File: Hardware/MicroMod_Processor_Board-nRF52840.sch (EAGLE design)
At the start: 33 parts, among them J1 MICROMOD-2222, U1 ARTEMIS_MODULESMD, U2 TSV524, U6 CH340E_MSOP10, Y1 32.768kHz

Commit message: Renamed eagle files appropriately
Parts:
- removed C11, C13: 15pF, SparkFun-Capacitors:15PF-0402T-50V-5%
- removed C20, C21: 0.1uF, SparkFun-Capacitors:0.1UF-0402T-16V-10%
- removed C28: 1.0nF, SparkFun-Capacitors:1.0NF/1000PF-0402_TIGHT-50V-10%
- removed R14, R6: 100k, SparkFun-Resistors:100KOHM-0402T-1/16W-1%
- removed R15: 220KOHM-0402T-1/16W-1%, SparkFun-Resistors:220KOHM-0402T-1/16W-1%
- removed R4, R5, R7: 150k, SparkFun-Resistors:150KOHM-0402T-1/16W-1%
- added C2, C3: 15pF, SparkFun-Capacitors:15PF-0402-50V-5%
- added C4, C5: 10uF, SparkFun-Capacitors:10UF-0402T-6.3V-20%
- added C6: 0.1uF, SparkFun-Capacitors:0.1UF-0402-16V-10%
- C1: device SparkFun-Capacitors:0.1UF-0402T-16V-10% -> SparkFun-Capacitors:0.1UF-0402-16V-10%
- R2, R3: value 100k -> 27; device SparkFun-Resistors:100KOHM-0402T-1/16W-1% -> SparkFun-Resistors:27OHM-0603-1/10W-1%
- U1: value ARTEMIS_MODULESMD -> W25QXX128MBIT-6X5; device SparkFun-IC-Microcontroller:ARTEMIS_MODULESMD -> SparkFun-MicroMod:W25QXX128MBIT-6X5
- U2: value TSV524 -> MDBT50Q; device OpAmp:TSV524 -> nrf52840:MDBT50Q
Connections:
- removed net ADC0_BUFF1: R3.2, U2G1.-IN, U2G1.OUT
- removed net ADC0_BUFF2: R3.1, R5.2, U2G2.+IN
- removed net ADC1_BUFF2: R6.1, R7.2, U2G3.+IN
- removed net ADC_BUFF1: R6.2, U2G4.-IN, U2G4.OUT
- removed net N$7: C11.2, U1.XO, Y1.2
- removed net SCALED_ADC0: U1.~AD32(SCCIO), U2G2.-IN, U2G2.OUT
- removed net SCALED_ADC1: U1.~AD35(TX1/I2SDAT/PDMCLK), U2G3.-IN, U2G3.OUT
- removed net SCALED_BATT_VIN/3: R2.1, R4.2, U1.~AD31(SCCCLK)
- new net N$1: R2.2, U2.D+
- new net N$3: R3.2, U2.D-
- net !RESET!: no longer C20.2, C28.1, R14.1, U1.!RST
- net !RTS: no longer C20.1, C21.1
- net 3.3V: now also C4.1, C5.1, C6.1, U1.VDD, U2.VDD, U2.VDDH; no longer R14.2, U1.VDD*2, U2G5.V+
- net 3.3V_EN: no longer U1.(SLNCE/I2SWCLK)D3
- net ADC0: no longer U2G1.+IN
- net ADC1: no longer U2G4.+IN
- net ADC_D+: no longer U1.~AD13(I2SBCLK/RX1)
- net ADC_D-: no longer U1.~AD12(PDMCLK/TX1)
- net BATT_VIN/3: no longer R2.2
- net BOOT: no longer C21.2, R15.2, U1.~BOOT(MOSI5/RX1/32KHZ)
- net CAM_PCLK: no longer U1.~AD11(PDMDATA)
- net CLKOUT: no longer U1.(SLSCK/SLSCL/CLKOUT)D0
- net CTS1: no longer U1.(CMPRF1/TRIG1/SCCCLK)D17
- net D0: no longer U1.(SLMOSI/SLSDA)D1
- net D1: no longer U1.(SLMISO)D2
- net GND: now also C2.1, C3.1, C4.2, C5.2, C6.2, U1.GND, U2.GND; no longer C11.1, C13.1, C28.2, R15.1, R4.1, R5.1, R7.1, U1.GND*6, U2G5.V-
- net GPIO0: no longer U1.AD16(TRIG0/SCCRST)
- net GPIO1: no longer U1.~AD33(SWO/32KHZ)
- net GPIO2: no longer U1.AD34(CMPRF2/PDMDATA)
- net GPIO3: no longer U1.(SCL2/SCK2)~D27
- net GPIO4: no longer U1.(MOSI2/I2SWCLK)~D28
- net GPIO5: no longer U1.~AD29(PDMDATA)
- net GPIO6: no longer U1.(ADCD1P/TX1/PDMCLK)D14
- net GPIO7: no longer U1.(ADCD1N/RX1/PDMDATA)D15
- net I2C_!INT!: no longer U1.(CMPIN1/SCCIO)~D18
- net LED_BUILTIN: no longer U1.(CMPRF0/SCCCLK/I2SBCLK)~D19
- net N$4: now also C3.2, U2.P0.00(XL1), Y1.1; no longer U1.XI
- net N$5: now also C2.2, U2.P0.01(XL2), Y1.2; no longer C13.2, Y1.1
- net PDM_CLK: no longer U1.(TX1/PDMCLK/SCCIO)~D37
- net PDM_DATA: no longer U1.(RX1/TRIG1/PDMDATA)D36
- net PWM0: no longer U1.(MOSI4)~D44
- net PWM1: no longer U1.(SWO/I2SDAT/PDMDATA)~D45
- net RTS1: no longer U1.(MOSI1/TX1/PDMCLK)D10
- net RX1: no longer U1.(SDA2/MISO2/RX1)~D25
- net RXI-0: no longer U1.~D49(RX0/SDA5/MISO5)
- net SCL: no longer U1.(SCL4/SCK4/TX1)~D39
- net SCL1: no longer U1.(SCL1/SCK1/TX1/SCCLK)D8
- net SDA: no longer U1.(SDA4/MISO4/RX1)D40
- net SDA1: no longer U1.(SDA1/MISO1/RX1/SCCIO)D9
- net SDIO_DATA1: no longer U1.(SCCRST)~D26
- net SDIO_DATA2: no longer U1.(RX1/SLINT)~D4
- net SPI_!CS!: no longer U1.(I2SWCLK/CMPOUT)~D23
- net SPI_!CS!1: no longer U1.(BLEIF_IRQ/SWO/I2SWCLK)D41
- net SPI_MISO: no longer U1.(PDMCLK/SWO)~D22, U1.(SDA0/MISO0/I2SDAT)~D6
- net SPI_MISO1: no longer U1.(SDA3/MISO3/RX1)~D43
- net SPI_MOSI: no longer U1.(MOSI0/CLKOUT)~D7
- net SPI_MOSI1: no longer U1.(MOSI3/RX1)D38
- net SPI_SCK: no longer U1.(SCL0/SCK0)~D5
- net SPI_SCK1: no longer U1.(SCL3/SCK3/TX1)~D42
- net SWDCK: now also U2.SWDCLK; no longer U1.D20(SWDCK/TX1)
- net SWDIO: now also U2.SWDIO; no longer U1.D21(SWDIO/RX1/SCCRST)
- net TX1: no longer U1.(TX1/32KHZ/SWO)~D24
- net TXO-0: no longer U1.~D48(TX0/SCL5/SCK5)
- net USB_D+: now also R2.1
- net USB_D-: now also R3.1
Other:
- note added: "128Mb Flash"
- note added: "MicroMod-nRF52840-Processor-Board"
- note added: "Paul Clark"
- note added: "Priyanka Makin"
- note added: "v1.0"
- note removed: "3.3V to 2V Scaling"
- note removed: "Artemis"
- note removed: "Bootloader Reset Circuit"
- note removed: "N. Seidle"
- note removed: "v1.2"
- moved on the sheet: C1, C17, C18, D2, D7, J1, R1, R2, R3, U6, Y1

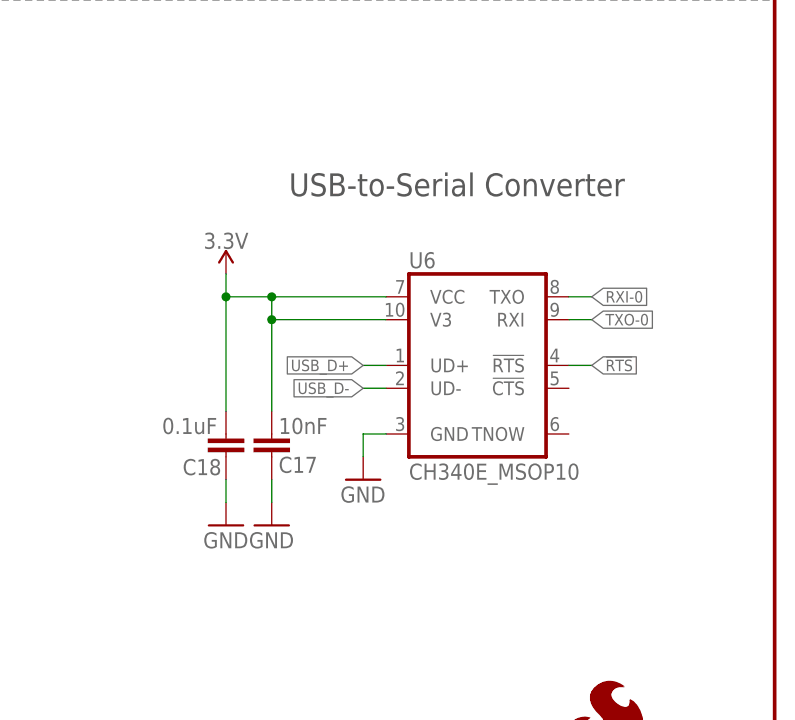
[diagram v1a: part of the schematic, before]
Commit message: Ripped up old traces
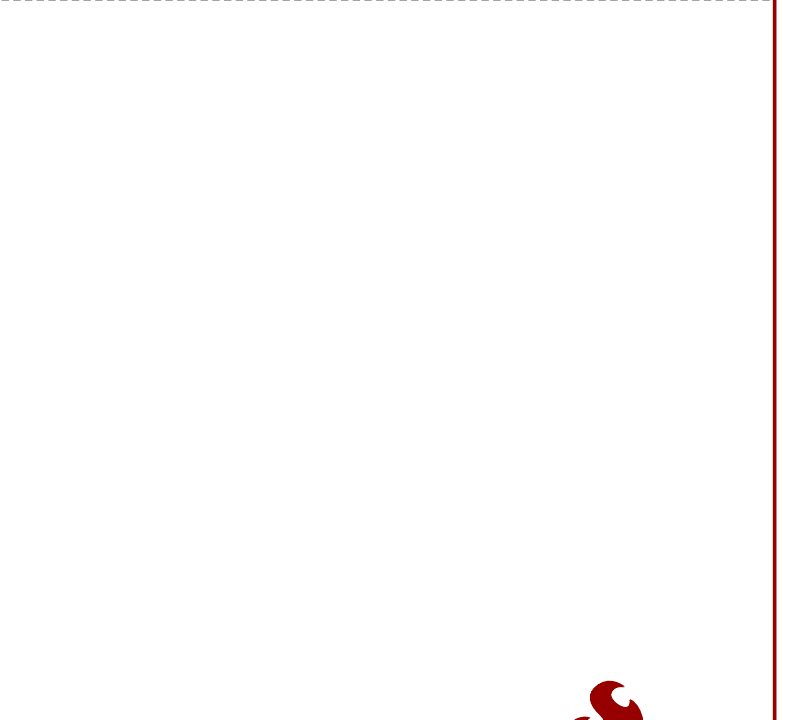
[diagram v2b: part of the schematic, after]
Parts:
- removed C17: 10nF, SparkFun-Capacitors:10NF-0402T-25V-10%
- removed C18: 0.1uF, SparkFun-Capacitors:0.1UF-0402T-16V-10%
- removed U6: CH340E_MSOP10, SparkFun-IC-Comms:CH340E_MSOP10
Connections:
- removed net !RTS: U6.!RTS
- removed net RXI-0: U6.TXO
- removed net TXO-0: U6.RXI
- net 3.3V: no longer C17.1, C18.1, U6.V3, U6.VCC
- net GND: no longer C17.2, C18.2, U6.GND
- net USB_D+: no longer U6.UD+
- net USB_D-: no longer U6.UD-
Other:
- note removed: "USB-to-Serial Converter"
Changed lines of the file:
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@@
 <part name="R1" library="SparkFun-Resistors" deviceset="1KOHM" device="-0402T-1/16W-1%" value="1k"/>
 <part name="GND3" library="SparkFun-PowerSymbols" deviceset="GND" device=""/>
-<part name="GND31" library="SparkFun-PowerSymbols" deviceset="GND" device=""/>
-<part name="C17" library="SparkFun-Capacitors" deviceset="10NF" device="-0402T-25V-10%" value="10nF"/>
-<part name="GND33" library="SparkFun-PowerSymbols" deviceset="GND" device=""/>
-<part name="C18" library="SparkFun-Capacitors" deviceset="0.1UF" device="-0402T-16V-10%" value="0.1uF"/>
-<part name="GND38" library="SparkFun-PowerSymbols" deviceset="GND" device=""/>
-<part name="SUPPLY26" library="SparkFun-PowerSymbols" deviceset="3.3V" device=""/>
-<part name="U6" library="SparkFun-IC-Comms" deviceset="CH340E" device="_MSOP10"/>
 <part name="FD1" library="SparkFun-Aesthetics" deviceset="FIDUCIAL" device="UFIDUCIAL" value="FIDUCIALUFIDUCIAL"/>
 <part name="FD2" library="SparkFun-Aesthetics" deviceset="FIDUCIAL" device="UFIDUCIAL" value="FIDUCIALUFIDUCIAL"/>
@@
 <sheet>
 <plain>
-<text x="396.494" y="116.586" size="2.54" layer="97" font="vector" align="center">USB-to-Serial Converter</text>
 <text x="53.594" y="271.526" size="2.54" layer="94" font="vector" align="center">MicroMod Connector</text>
 <wire x1="0" y1="137.16" x2="104.14" y2="137.16" width="0.2032" layer="97" style="longdash"/>
@@
 <attribute name="VALUE" x="60.96" y="83.566" size="1.778" layer="96" align="top-center"/>
 </instance>
-<instance part="GND31" gate="1" x="370.84" y="78.74" smashed="yes">
-<attribute name="VALUE" x="368.3" y="76.2" size="1.778" layer="96"/>
-</instance>
-<instance part="C17" gate="G$1" x="375.92" y="86.36" smashed="yes">
-<attribute name="NAME" x="376.682" y="84.582" size="1.778" layer="95"/>
-<attribute name="VALUE" x="376.682" y="88.9" size="1.778" layer="96"/>
-</instance>
-<instance part="GND33" gate="1" x="375.92" y="78.74" smashed="yes">
-<attribute name="VALUE" x="373.38" y="76.2" size="1.778" layer="96"/>
-</instance>
-<instance part="C18" gate="G$1" x="370.84" y="86.36" smashed="yes">
-<attribute name="NAME" x="366.014" y="84.328" size="1.778" layer="95"/>
-<attribute name="VALUE" x="363.728" y="88.9" size="1.778" layer="96"/>
-</instance>
-<instance part="GND38" gate="1" x="386.08" y="83.82" smashed="yes">
-<attribute name="VALUE" x="383.54" y="81.28" size="1.778" layer="96"/>
-</instance>
-<instance part="SUPPLY26" gate="G$1" x="370.84" y="106.68" smashed="yes">
-<attribute name="VALUE" x="370.84" y="109.474" size="1.778" layer="96" align="bottom-center"/>
-</instance>
-<instance part="U6" gate="U1" x="398.78" y="96.52" smashed="yes">
-<attribute name="NAME" x="391.16" y="107.315" size="1.778" layer="95"/>
-<attribute name="VALUE" x="391.16" y="83.82" size="1.778" layer="96"/>
-</instance>
 <instance part="FD1" gate="G$1" x="429.26" y="25.4" smashed="yes"/>
 <instance part="FD2" gate="G$1" x="426.72" y="25.4" smashed="yes"/>
@@
 <net name="3.3V" class="0">
 <segment>
-<pinref part="C18" gate="G$1" pin="1"/>
-<wire x1="370.84" y1="106.68" x2="370.84" y2="104.14" width="0.1524" layer="91"/>
-<wire x1="370.84" y1="104.14" x2="370.84" y2="91.44" width="0.1524" layer="91"/>
-<wire x1="388.62" y1="104.14" x2="375.92" y2="104.14" width="0.1524" layer="91"/>
-<junction x="370.84" y="104.14"/>
-<pinref part="SUPPLY26" gate="G$1" pin="3.3V"/>
-<pinref part="U6" gate="U1" pin="VCC"/>
-<wire x1="375.92" y1="104.14" x2="370.84" y2="104.14" width="0.1524" layer="91"/>
-<wire x1="388.62" y1="101.6" x2="375.92" y2="101.6" width="0.1524" layer="91"/>
-<pinref part="C17" gate="G$1" pin="1"/>
-<wire x1="375.92" y1="91.44" x2="375.92" y2="101.6" width="0.1524" layer="91"/>
-<pinref part="U6" gate="U1" pin="V3"/>
-<wire x1="375.92" y1="101.6" x2="375.92" y2="104.14" width="0.1524" layer="91"/>
-<junction x="375.92" y="101.6"/>
-<junction x="375.92" y="104.14"/>
-</segment>
-<segment>
 <wire x1="12.7" y1="241.3" x2="12.7" y2="254" width="0.1524" layer="91"/>
 <wire x1="30.48" y1="241.3" x2="12.7" y2="241.3" width="0.1524" layer="91"/>
@@
 <pinref part="GND3" gate="1" pin="GND"/>
 <wire x1="60.96" y1="86.36" x2="60.96" y2="88.9" width="0.1524" layer="91"/>
-</segment>
-<segment>
-<wire x1="370.84" y1="83.82" x2="370.84" y2="81.28" width="0.1524" layer="91"/>
-<pinref part="GND31" gate="1" pin="GND"/>
-<pinref part="C18" gate="G$1" pin="2"/>
-</segment>
-<segment>
-<pinref part="C17" gate="G$1" pin="2"/>
-<pinref part="GND33" gate="1" pin="GND"/>
-<wire x1="375.92" y1="81.28" x2="375.92" y2="83.82" width="0.1524" layer="91"/>
-</segment>
-<segment>
-<wire x1="388.62" y1="88.9" x2="386.08" y2="88.9" width="0.1524" layer="91"/>
-<wire x1="386.08" y1="88.9" x2="386.08" y2="86.36" width="0.1524" layer="91"/>
-<pinref part="GND38" gate="1" pin="GND"/>
-<pinref part="U6" gate="U1" pin="GND"/>
 </segment>
 <segment>
@@
 </segment>
 </net>
-<net name="RXI-0" class="0">
-<segment>
-<label x="411.48" y="104.14" size="1.27" layer="95" font="vector" xref="yes"/>
-<wire x1="408.94" y1="104.14" x2="411.48" y2="104.14" width="0.1524" layer="91"/>
-<pinref part="U6" gate="U1" pin="TXO"/>
-</segment>
-</net>
-<net name="TXO-0" class="0">
-<segment>
-<label x="411.48" y="101.6" size="1.27" layer="95" font="vector" xref="yes"/>
-<wire x1="408.94" y1="101.6" x2="411.48" y2="101.6" width="0.1524" layer="91"/>
-<pinref part="U6" gate="U1" pin="RXI"/>
-</segment>
-</net>
-<net name="!RTS" class="0">
-<segment>
-<wire x1="408.94" y1="96.52" x2="411.48" y2="96.52" width="0.1524" layer="91"/>
-<label x="411.48" y="96.52" size="1.27" layer="95" xref="yes"/>
-<pinref part="U6" gate="U1" pin="!RTS"/>
-</segment>
-</net>
 <net name="USB_D-" class="0">
 <segment>
@@
 </segment>
 <segment>
-<wire x1="388.62" y1="93.98" x2="386.08" y2="93.98" width="0.1524" layer="91"/>
-<pinref part="U6" gate="U1" pin="UD-"/>
-<label x="386.08" y="93.98" size="1.27" layer="95" rot="R180" xref="yes"/>
-</segment>
-<segment>
 <pinref part="R3" gate="G$1" pin="1"/>
 <wire x1="152.4" y1="236.22" x2="149.86" y2="236.22" width="0.1524" layer="91"/>
@@
 </segment>
 <segment>
-<wire x1="386.08" y1="96.52" x2="388.62" y2="96.52" width="0.1524" layer="91"/>
-<pinref part="U6" gate="U1" pin="UD+"/>
-<label x="386.08" y="96.52" size="1.27" layer="95" rot="R180" xref="yes"/>
-</segment>
-<segment>

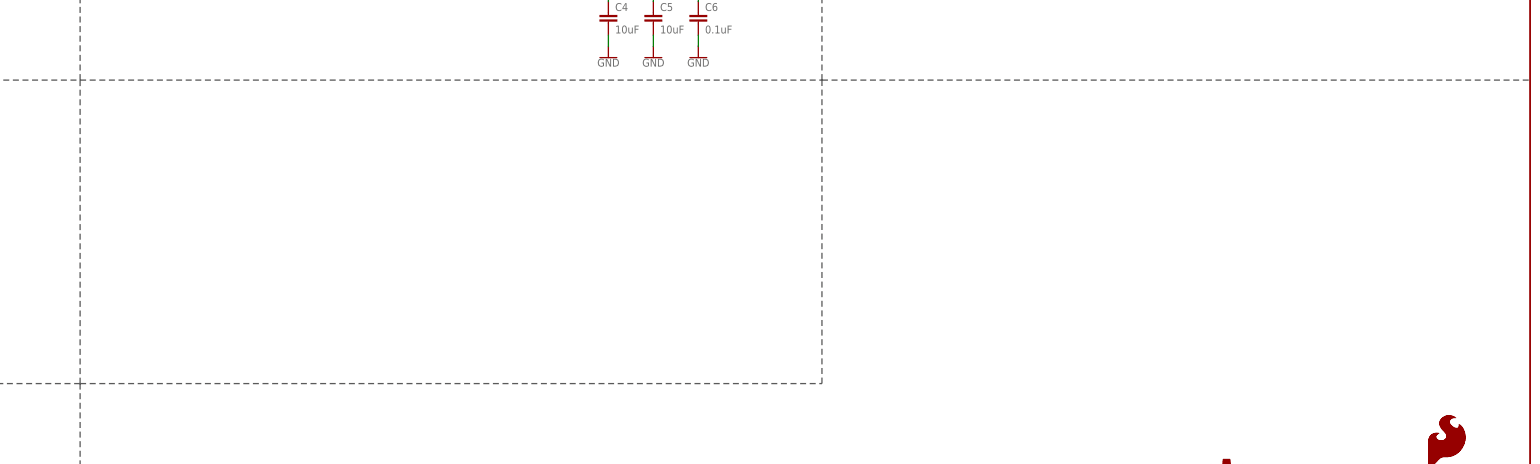
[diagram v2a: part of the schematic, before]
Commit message: Removed some dividing lines in schematic
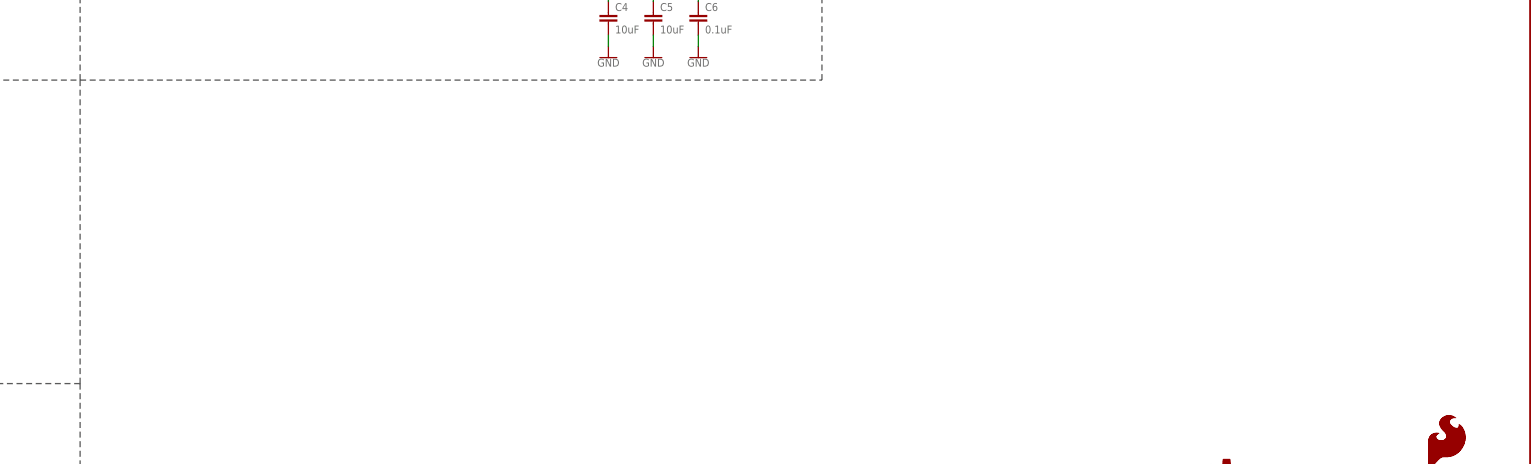
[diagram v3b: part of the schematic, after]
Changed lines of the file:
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@@
 <wire x1="104.14" y1="137.16" x2="271.78" y2="137.16" width="0.2032" layer="97" style="longdash"/>
 <wire x1="271.78" y1="137.16" x2="271.78" y2="279.4" width="0.2032" layer="97" style="longdash"/>
-<wire x1="271.78" y1="137.16" x2="431.8" y2="137.16" width="0.2032" layer="97" style="longdash"/>
 <wire x1="104.14" y1="137.16" x2="104.14" y2="68.58" width="0.2032" layer="97" style="longdash"/>
 <wire x1="104.14" y1="68.58" x2="104.14" y2="0" width="0.2032" layer="97" style="longdash"/>
 <wire x1="104.14" y1="68.58" x2="0" y2="68.58" width="0.2032" layer="97" style="longdash"/>
-<wire x1="104.14" y1="68.58" x2="271.78" y2="68.58" width="0.2032" layer="97" style="longdash"/>
-<wire x1="271.78" y1="68.58" x2="271.78" y2="137.16" width="0.2032" layer="97" style="longdash"/>
 <text x="56.134" y="124.206" size="2.54" layer="94" font="vector" align="center">Status LED</text>
 <text x="51.054" y="149.606" size="2.54" layer="97" font="vector" align="center">Vin: 1.755 - 3.63V</text>
